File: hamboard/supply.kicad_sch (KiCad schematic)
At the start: 22 parts, among them J9 Barrel_Jack, Q5 AO3401A, U6 AMS1117-1.2, U7 xl1509-3v3, U8 AIC1747-28

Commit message: board: bom
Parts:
- C30: value 470uF/50V -> 680uF/50V; footprint Capacitor_SMD:CP_Elec_16x17.5 -> Capacitor_THT:CP_Radial_D13.0mm_P5.00mm; LCSC (none) -> C399014
- C31: value C -> 100nF
- C32: footprint Capacitor_SMD:CP_Elec_10x12.5 -> Capacitor_SMD:CP_Elec_10x10.5; LCSC (none) -> C310832
- D3: value SD24_SOD323 -> SD24_SOD523; footprint Diode_SMD:D_SOD-323 -> Diode_SMD:D_SOD-523; LCSC (none) -> C558432
- D4: value D_Zener -> D_Zener 25V; LCSC (none) -> C188545
- D5: footprint lib:DIOM6859X262N -> Diode_SMD:D_SMA; LCSC (none) -> C64998; MANUFACTURER Taiwan Semiconductor -> (none); MAXIMUM_PACKAGE_HEIGHT 2.62 mm -> (none); PARTREV Q2102 -> (none); STANDARD IPC-7351B -> (none)
- F1: value Polyfuse -> Polyfuse 24V/4A; footprint (none) -> Fuse:Fuse_2920_7451Metric; LCSC (none) -> C2982292
- J9: LCSC (none) -> C381116
- L1: LCSC (none) -> C408455
- Q5: LCSC (none) -> C700954
- R19: value R -> 12k
- U6: LCSC (none) -> C2992568
- U7: LCSC (none) -> C2681226
- U8: LCSC (none) -> C238238
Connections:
- net GND: now also U7.4 (ON/OFF)
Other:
- moved on the sheet: C30, C31

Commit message: first pcb layout
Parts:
- removed TP6: TestPoint, TestPoint:TestPoint_Pad_D1.5mm, symbol Connector:TestPoint
- D4: footprint Capacitor_SMD:CP_Elec_8x10 -> Diode_SMD:D_MiniMELF; LCSC C188545 -> C118705
- D5: footprint Diode_SMD:D_SMA -> DIOM6859X262N; symbol ss33:SS33 -> hamboard:SS33; MANUFACTURER (none) -> Taiwan Semiconductor; MAXIMUM_PACKAGE_HEIGHT (none) -> 2.62 mm; PARTREV (none) -> Q2102; STANDARD (none) -> IPC-7351B
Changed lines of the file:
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@@
-    (stroke (width 0) (type default) (color 0 0 0 0))
-  )
-  (wire (pts (xy 92.71 118.11) (xy 92.71 123.19))
     (stroke (width 0) (type default) (color 0 0 0 0))
   )
@@
     (pin "2")
   )
-  (symbol (lib_id "ss33:SS33") (at 223.52 64.77 90) (unit 1)
+  (symbol (lib_id "hamboard:SS33") (at 223.52 64.77 90) (unit 1)
     (in_bom yes) (on_board yes) (fields_autoplaced)
     (property "Reference" "D5" (id 0) (at 226.06 63.4999 90)
@@
       (effects (font (size 1.27 1.27)) (justify right))
     )
-    (property "Footprint" "Diode_SMD:D_SMA" (id 2) (at 223.52 64.77 0)
+    (property "Footprint" "DIOM6859X262N" (id 2) (at 219.71 66.04 0)
       (effects (font (size 1.27 1.27)) (justify left bottom) hide)
     )
@@
     (property "LCSC" "C64998" (id 8) (at 223.52 64.77 90)
       (effects (font (size 1.27 1.27)) hide)
+    )
+    (property "PARTREV" "Q2102" (id 5) (at 219.075 65.405 0)
+      (effects (font (size 1.27 1.27)) (justify left bottom) hide)
+    )
+    (property "STANDARD" "IPC-7351B" (id 6) (at 220.98 66.04 0)
+      (effects (font (size 1.27 1.27)) (justify left bottom) hide)
+    )
+    (property "MANUFACTURER" "Taiwan Semiconductor" (id 7) (at 220.98 65.405 0)
+      (effects (font (size 1.27 1.27)) (justify left bottom) hide)
+    )
+    (property "MAXIMUM_PACKAGE_HEIGHT" "2.62 mm" (id 9) (at 222.25 64.77 0)
+      (effects (font (size 1.27 1.27)) (justify left bottom) hide)
     )
     (pin "A")
@@
       (effects (font (size 1.27 1.27)) (justify left))
     )
-    (property "Footprint" "Capacitor_SMD:CP_Elec_8x10" (id 2) (at 113.03 58.42 0)
+    (property "Footprint" "Diode_SMD:D_MiniMELF" (id 2) (at 113.03 58.42 0)
       (effects (font (size 1.27 1.27)) hide)
     )
@@
       (effects (font (size 1.27 1.27)) hide)
     )
-    (property "LCSC" "C188545" (id 4) (at 113.03 58.42 90)
+    (property "LCSC" "C118705" (id 4) (at 113.03 58.42 90)
       (effects (font (size 1.27 1.27)) hide)
     )
@@
     (pin "1")
   )
-  (symbol (lib_id "power:+1V2") (at 92.71 118.11 0) (unit 1)
-    (in_bom yes) (on_board yes) (fields_autoplaced)
-    (property "Reference" "#PWR073" (id 0) (at 92.71 121.92 0)
-      (effects (font (size 1.27 1.27)) hide)
-    )
-    (property "Value" "+1V2" (id 1) (at 92.71 113.03 0))
-    (property "Footprint" "" (id 2) (at 92.71 118.11 0)
-      (effects (font (size 1.27 1.27)) hide)
-    )
-    (property "Datasheet" "" (id 3) (at 92.71 118.11 0)
+  (symbol (lib_id "power:+1V2") (at 101.6 120.65 0) (unit 1)
+    (in_bom yes) (on_board yes) (fields_autoplaced)
+    (property "Reference" "#PWR073" (id 0) (at 101.6 124.46 0)
+      (effects (font (size 1.27 1.27)) hide)
+    )
+    (property "Value" "+1V2" (id 1) (at 101.6 115.57 0))
+    (property "Footprint" "" (id 2) (at 101.6 120.65 0)
+      (effects (font (size 1.27 1.27)) hide)
+    )
+    (property "Datasheet" "" (id 3) (at 101.6 120.65 0)
       (effects (font (size 1.27 1.27)) hide)
     )
@@
       (effects (font (size 1.27 1.27)) hide)
     )
-    (pin "1")
-  )
-  (symbol (lib_id "Connector:TestPoint") (at 101.6 120.65 0) (unit 1)
-    (in_bom yes) (on_board yes) (fields_autoplaced)
-    (property "Reference" "TP6" (id 0) (at 104.14 116.0779 0)
-      (effects (font (size 1.27 1.27)) (justify left))
-    )
-    (property "Value" "TestPoint" (id 1) (at 104.14 118.6179 0)
-      (effects (font (size 1.27 1.27)) (justify left))
-    )
-    (property "Footprint" "TestPoint:TestPoint_Pad_D1.5mm" (id 2) (at 106.68 120.65 0)
-      (effects (font (size 1.27 1.27)) hide)
-    )
-    (property "Datasheet" "~" (id 3) (at 106.68 120.65 0)
-      (effects (font (size 1.27 1.27)) hide)
-    )

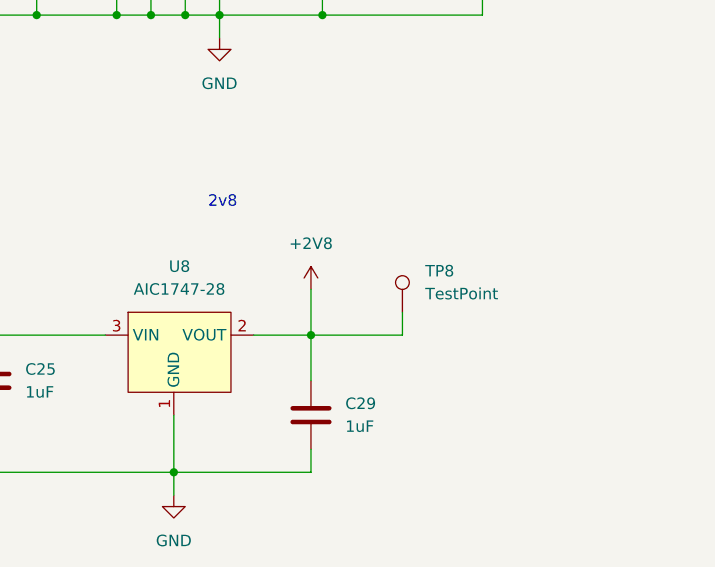
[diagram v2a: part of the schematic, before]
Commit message: pcb: added screws and rerouted everything
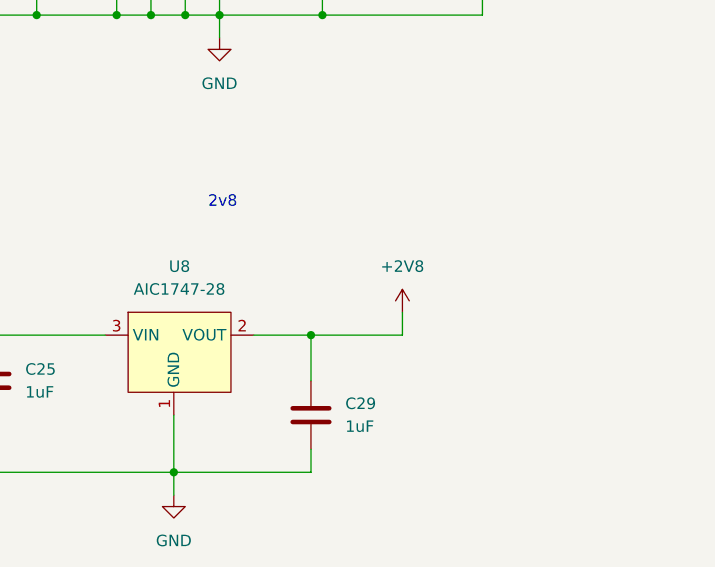
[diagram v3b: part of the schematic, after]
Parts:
- removed TP8: TestPoint, TestPoint:TestPoint_Pad_D1.5mm, symbol Connector:TestPoint
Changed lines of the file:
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@@
-    (stroke (width 0) (type default) (color 0 0 0 0))
-  )
-  (wire (pts (xy 222.25 102.87) (xy 222.25 107.95))
     (stroke (width 0) (type default) (color 0 0 0 0))
   )
@@
     (pin "2")
   )
-  (symbol (lib_id "power:+2V8") (at 222.25 102.87 0) (unit 1)
-    (in_bom yes) (on_board yes) (fields_autoplaced)
-    (property "Reference" "#PWR082" (id 0) (at 222.25 106.68 0)
-      (effects (font (size 1.27 1.27)) hide)
-    )
-    (property "Value" "+2V8" (id 1) (at 222.25 97.79 0))
-    (property "Footprint" "" (id 2) (at 222.25 102.87 0)
-      (effects (font (size 1.27 1.27)) hide)
-    )
-    (property "Datasheet" "" (id 3) (at 222.25 102.87 0)
+  (symbol (lib_id "power:+2V8") (at 232.41 105.41 0) (unit 1)
+    (in_bom yes) (on_board yes) (fields_autoplaced)
+    (property "Reference" "#PWR082" (id 0) (at 232.41 109.22 0)
+      (effects (font (size 1.27 1.27)) hide)
+    )
+    (property "Value" "+2V8" (id 1) (at 232.41 100.33 0))
+    (property "Footprint" "" (id 2) (at 232.41 105.41 0)
+      (effects (font (size 1.27 1.27)) hide)
+    )
+    (property "Datasheet" "" (id 3) (at 232.41 105.41 0)
       (effects (font (size 1.27 1.27)) hide)
     )
@@
       (effects (font (size 1.27 1.27)) hide)
     )
-    (pin "1")
-  )
-  (symbol (lib_id "Connector:TestPoint") (at 232.41 105.41 0) (unit 1)
-    (in_bom yes) (on_board yes) (fields_autoplaced)
-    (property "Reference" "TP8" (id 0) (at 234.95 100.8379 0)
-      (effects (font (size 1.27 1.27)) (justify left))
-    )
-    (property "Value" "TestPoint" (id 1) (at 234.95 103.3779 0)
-      (effects (font (size 1.27 1.27)) (justify left))
-    )
-    (property "Footprint" "TestPoint:TestPoint_Pad_D1.5mm" (id 2) (at 237.49 105.41 0)
-      (effects (font (size 1.27 1.27)) hide)
-    )
-    (property "Datasheet" "~" (id 3) (at 237.49 105.41 0)
-      (effects (font (size 1.27 1.27)) hide)
-    )

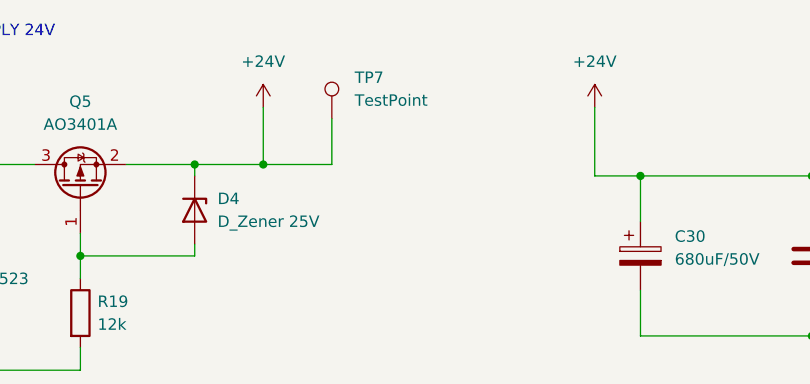
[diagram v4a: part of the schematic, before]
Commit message: board: fixed esp heat pads
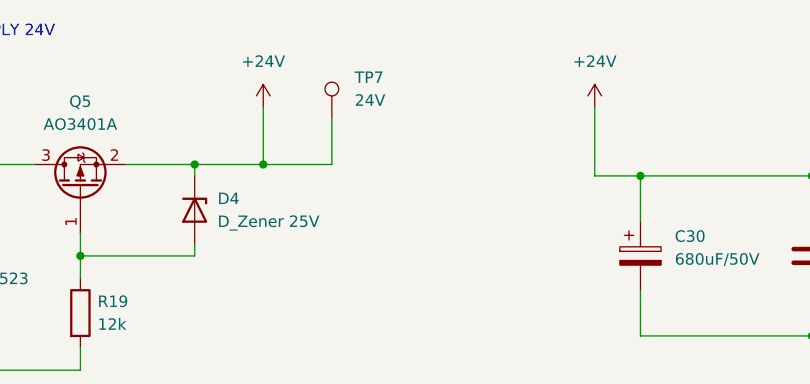
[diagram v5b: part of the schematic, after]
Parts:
- D3: footprint Diode_SMD:D_SOD-523 -> Diode_SMD:D_SOD-323
- TP7: value TestPoint -> 24V
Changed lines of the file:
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@@
       (effects (font (size 1.27 1.27)) hide)
     )
-    (property "Datasheet" "https://datasheet.lcsc.com/lcsc/1912111437_Xunda-RK6871HMJ212RB_C399014.pdf" (id 3) (at 162.56 63.5 0)
+    (property "Datasheet" "~" (id 3) (at 162.56 63.5 0)
       (effects (font (size 1.27 1.27)) hide)
     )
@@
       (effects (font (size 1.27 1.27)) hide)
     )
-    (property "Datasheet" "https://datasheet.lcsc.com/lcsc/2202251830_ROQANG-RVE1V331M1010_C310832.pdf" (id 3) (at 241.3 64.77 0)
+    (property "Datasheet" "~" (id 3) (at 241.3 64.77 0)
       (effects (font (size 1.27 1.27)) hide)
     )
@@
       (effects (font (size 1.27 1.27)) (justify left))
     )
-    (property "Value" "TestPoint" (id 1) (at 130.81 46.2279 0)
+    (property "Value" "24V" (id 1) (at 130.81 46.2279 0)
       (effects (font (size 1.27 1.27)) (justify left))
     )
@@
       (effects (font (size 1.27 1.27)) (justify left) hide)
     )
-    (property "Datasheet" "https://datasheet.lcsc.com/lcsc/2204011730_Shenzhen-JDT-Fuse-ASMD2920-400-24V_C2982292.pdf" (id 3) (at 66.04 53.34 0)
+    (property "Datasheet" "~" (id 3) (at 66.04 53.34 0)
       (effects (font (size 1.27 1.27)) hide)
     )
@@
       (effects (font (size 1.27 1.27)) hide)
     )
-    (property "Datasheet" "" (id 3) (at 232.41 58.42 0)
+    (property "Datasheet" "~" (id 3) (at 232.41 58.42 0)
       (effects (font (size 1.27 1.27)) hide)
     )
@@
       (effects (font (size 1.27 1.27)) (justify right))
     )
-    (property "Footprint" "Diode_SMD:D_SOD-523" (id 2) (at 83.82 64.77 0)
-      (effects (font (size 1.27 1.27)) hide)
-    )
-    (property "Datasheet" "https://datasheet.lcsc.com/lcsc/2005211234_TECH-PUBLIC-TPPESD24VS1UB_C558432.pdf" (id 3) (at 78.74 64.77 0)
-      (effects (font (size 1.27 1.27)) hide)
-    )
+    (property "Footprint" "Diode_SMD:D_SOD-323" (id 2) (at 83.82 64.77 0)
+      (effects (font (size 1.27 1.27)) hide)
+    )
+    (property "Datasheet" "https://www.littelfuse.com/~/media/electronics/datasheets/tvs_diode_arrays/littelfuse_tvs_diode_array_sd_c_datasheet.pdf.pdf" (id 3) (at 78.74 64.77 0)
+      (effects (font (size 1.27 1.27)) hide)
+    )
